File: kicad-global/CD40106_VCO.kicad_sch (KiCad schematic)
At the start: 46 parts, among them J1 1V/Oct, J2 FM, J3 PWM_CV, J4 Saw, J5 Square, Q1 BC558, Q2 BC548, U1 TL074, U2 40106

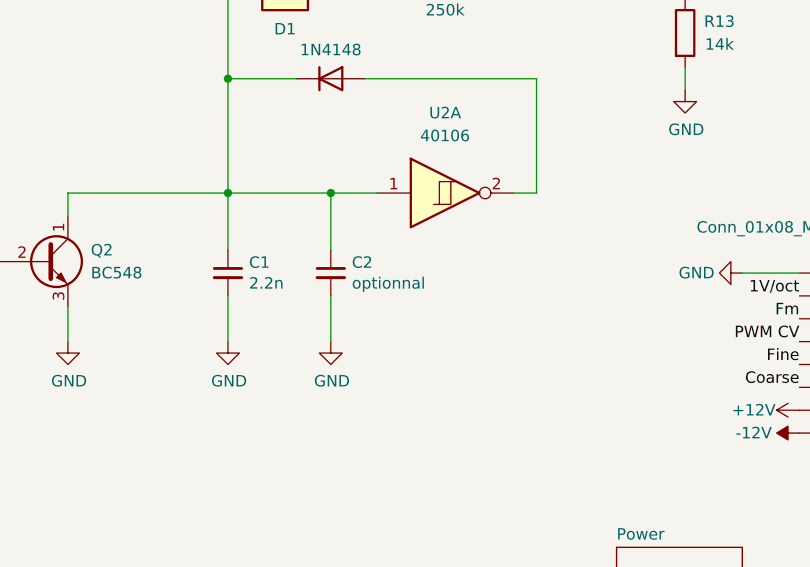
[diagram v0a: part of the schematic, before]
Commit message: update components
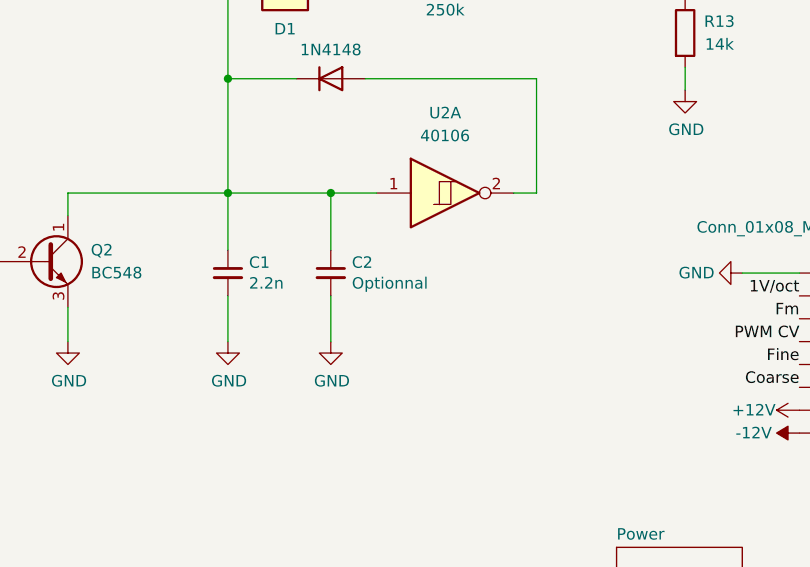
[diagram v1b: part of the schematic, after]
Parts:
- C1: footprint Capacitor_THT:C_Disc_D7.0mm_W2.5mm_P5.00mm -> Capacitor_THT:C_Rect_L7.0mm_W6.5mm_P5.00mm; Comments (none) -> Mica capacitor for stability; manf (none) -> Cornell Dubilier; manf# (none) -> CD16FD222JO3F
- C2: value optionnal -> Optionnal; footprint Capacitor_THT:C_Disc_D7.0mm_W2.5mm_P5.00mm -> Capacitor_THT:C_Rect_L7.0mm_W6.5mm_P5.00mm; Comments (none) -> Mica capacitor for stability; manf (none) -> Cornell Dubilier; manf# (none) -> CD16FD222JO3F
- lvl_Trim: Comments (none) -> Use multi turn Cermet style 3296 pots
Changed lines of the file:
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@@
       (effects (font (size 1.27 1.27)) (justify left))
     )
-    (property "Footprint" "Capacitor_THT:C_Disc_D7.0mm_W2.5mm_P5.00mm" (at 133.35 119.38 0)
+    (property "Footprint" "Capacitor_THT:C_Rect_L7.0mm_W6.5mm_P5.00mm" (at 133.35 119.38 0)
       (effects (font (size 1.27 1.27)) hide)
     )
     (property "Datasheet" "~" (at 133.35 119.38 0)
+      (effects (font (size 1.27 1.27)) hide)
+    )
+    (property "manf" "Cornell Dubilier" (at 133.35 119.38 0)
+      (effects (font (size 1.27 1.27)) hide)
+    )
+    (property "manf#" "CD16FD222JO3F" (at 133.35 119.38 0)
+      (effects (font (size 1.27 1.27)) hide)
+    )
+    (property "Comments" "Mica capacitor for stability" (at 133.35 119.38 0)
       (effects (font (size 1.27 1.27)) hide)
     )
@@
     )
     (property "Datasheet" "~" (at 80.01 152.4 0)
+      (effects (font (size 1.27 1.27)) hide)
+    )
+    (property "manf" "" (at 80.01 152.4 90)
+      (effects (font (size 1.27 1.27)) hide)
+    )
+    (property "manf#" "" (at 80.01 152.4 90)
+      (effects (font (size 1.27 1.27)) hide)
+    )
+    (property "Comments" "Use multi turn Cermet style 3296 pots " (at 80.01 152.4 90)
       (effects (font (size 1.27 1.27)) hide)
     )
@@
     )
   )
-  (symbol (lib_id "Device:C_Small") (at 144.78 119.38 0) (unit 1)
-    (in_bom yes) (on_board yes) (dnp no)
-    (property "Reference" "C2" (at 147.1168 118.2116 0)
-      (effects (font (size 1.27 1.27)) (justify left))
-    )
-    (property "Value" "optionnal" (at 147.1168 120.523 0)
-      (effects (font (size 1.27 1.27)) (justify left))
-    )
-    (property "Footprint" "Capacitor_THT:C_Disc_D7.0mm_W2.5mm_P5.00mm" (at 144.78 119.38 0)
-      (effects (font (size 1.27 1.27)) hide)
-    )
-    (property "Datasheet" "~" (at 144.78 119.38 0)
-      (effects (font (size 1.27 1.27)) hide)
-    )
-    (pin "1")
-    (pin "2")
-    (instances
-      (project "CD40106_VCO"
-        (path "/fea7c5d1-76d6-41a0-b5e3-29889dbb8ce0"
-          (reference "C2") (unit 1)
-        )
-      )
-    )
-  )
   (symbol (lib_id "Transistor_BJT:BC558") (at 96.52 125.73 0) (unit 1)
     (in_bom yes) (on_board yes) (dnp no) (fields_autoplaced)
@@
         )
       )
+    )
+  )
+  (symbol (lib_id "Device:C_Small") (at 144.78 119.38 0) (unit 1)
+    (in_bom yes) (on_board yes) (dnp no)
+    (property "Reference" "C2" (at 147.1168 118.2116 0)
+      (effects (font (size 1.27 1.27)) (justify left))
+    )
+    (property "Value" "Optionnal" (at 147.1168 120.523 0)
+      (effects (font (size 1.27 1.27)) (justify left))
+    )
+    (property "Footprint" "Capacitor_THT:C_Rect_L7.0mm_W6.5mm_P5.00mm" (at 144.78 119.38 0)
+      (effects (font (size 1.27 1.27)) hide)
+    )
+    (property "Datasheet" "~" (at 144.78 119.38 0)
+      (effects (font (size 1.27 1.27)) hide)
+    )
+    (property "manf" "Cornell Dubilier" (at 144.78 119.38 0)
+      (effects (font (size 1.27 1.27)) hide)
+    )
+    (property "manf#" "CD16FD222JO3F" (at 144.78 119.38 0)
+      (effects (font (size 1.27 1.27)) hide)
+    )
+    (property "Comments" "Mica capacitor for stability" (at 144.78 119.38 0)
+      (effects (font (size 1.27 1.27)) hide)
+    )
+    (pin "1")
+    (pin "2")
+    (instances
+      (project "CD40106_VCO"
+        (path "/fea7c5d1-76d6-41a0-b5e3-29889dbb8ce0"
+          (reference "C2") (unit 1)
+        )
+      )

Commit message: finished v1 of module
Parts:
- removed J1: 1V/Oct, Synth:Thonkiconn, symbol Connector:AudioJack2_SwitchT
- removed J2: FM, Synth:Thonkiconn, symbol Connector:AudioJack2_SwitchT
- removed J3: PWM_CV, Synth:Thonkiconn, symbol Connector:AudioJack2_SwitchT
- removed J4: Saw, Synth:Thonkiconn, symbol Connector:AudioJack2_SwitchT
- removed J5: Square, Synth:Thonkiconn, symbol Connector:AudioJack2_SwitchT
- removed J? (x2): Conn_01x08_Female, Connector_PinSocket_2.54mm:PinSocket_1x08_P2.54mm_Vertical, symbol Connector:Conn_01x08_Female
- removed J? (x2): Conn_01x08_Male, Connector_PinHeader_2.54mm:PinHeader_1x08_P2.54mm_Vertical, symbol Connector:Conn_01x08_Male
- added D1: 1N4148, Diode_THT:D_DO-35_SOD27_P7.62mm_Horizontal, symbol Device:D
- added J13: PWM_CV, Kicad-perso:Thonkiconn, symbol Kicad-perso:AudioJack_Switch
- added J13: CV, Kicad-perso:Thonkiconn, symbol Kicad-perso:AudioJack_Switch
- added J13: Square, Kicad-perso:Thonkiconn, symbol Kicad-perso:AudioJack_Switch
- added J13: Sync, Kicad-perso:Thonkiconn, symbol Kicad-perso:AudioJack_Switch
- added J13: Saw, Kicad-perso:Thonkiconn, symbol Kicad-perso:AudioJack_Switch
- added J13: FM, Kicad-perso:Thonkiconn, symbol Kicad-perso:AudioJack_Switch
- added J3 (x2): Conn_Circuit, Connector_PinSocket_2.54mm:PinSocket_1x08_P2.54mm_Vertical, symbol Connector_Generic:Conn_01x08
- added J5 (x2): Conn_Jack, Connector_PinHeader_2.54mm:PinHeader_1x08_P2.54mm_Vertical, symbol Connector_Generic:Conn_01x08
- added TP1 (x2): TestPoint, TestPoint:TestPoint_Plated_Hole_D2.0mm, symbol Connector:TestPoint
- C1: value 2.2n -> 2.2nF; footprint Capacitor_THT:C_Rect_L7.0mm_W6.5mm_P5.00mm -> Kicad-perso:Mica Disc Cap
- C2: footprint Capacitor_THT:C_Rect_L7.0mm_W6.5mm_P5.00mm -> Capacitor_THT:C_Disc_D7.0mm_W2.5mm_P5.00mm; Comments Mica capacitor for stability -> If you don't have a mica capacitor, just use a regular cera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; manf Cornell Dubilier -> (none); manf# CD16FD222JO3F -> (none)
- C3: value 1u -> 1uF
- FM_LVL1, PWM1, PWM_CV_LVL1: footprint Synth:Pot-bourns-alpha -> Kicad-perso:Pot-bourns-alpha
- H3: renamed from H1; footprint Synth:Doepfer Mounting hole -> Kicad-perso:Doepfer Mounting hole
- H4: renamed from H2; footprint Synth:Doepfer Mounting hole -> Kicad-perso:Doepfer Mounting hole
- H5: renamed from H3; footprint Synth:Doepfer Mounting hole -> Kicad-perso:Doepfer Mounting hole
- H6: renamed from H4; footprint Synth:Doepfer Mounting hole -> Kicad-perso:Doepfer Mounting hole
- TH1, TH2, TH3, TH4: footprint (none) -> Kicad-perso:Therm_Disc_D6.5mm_W2.5mm_P3.50mm; manf (none) -> THINKING; manf# (none) -> ATTC-5100
- U2: value 40106 -> CD40106; footprint (none) -> Package_DIP:DIP-14_W7.62mm_LongPads; manf (none) -> Nexperia; manf# (none) -> CD40106BE
- gave numbers to parts that had none: 2
- renumbered D1 to D2, R4 to R1, R13 to R10, R14 to R11, R15 to R12, R16 to R13, R17 to R14, R18 to R15, R5 to R2, R6 to R3, R7 to R4, R8 to R5, R9 to R6, R10 to R7, R11 to R8, R12 to R9, lvl_Trim to lvl_Trim1
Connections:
- net Octave switch/Fine is gone; now on net Fine: R2.2
- net +12V: now also PWM1.3, J3.7 (Pin_7), J5.7 (Pin_7); no longer PWM1.1
- net -12V: now also PWM1.1, J3.8 (Pin_8), J5.8 (Pin_8); no longer PWM1.3
- net 1V/oct: now also J13.T, J3.2 (Pin_2), J5.2 (Pin_2)
- net Fine: now also J3.5 (Pin_5), J5.5 (Pin_5)
- net Fm: now also J3.3 (Pin_3), J5.3 (Pin_3)
- net GND: now also J13.S, J13.S, J13.S, J13.S, J13.S, J13.S, J13.TN, J13.TN, J13.TN, J3.1 (Pin_1), J3.1 (Pin_1), J3.8 (Pin_8), J5.1 (Pin_1), J5.1 (Pin_1), J5.8 (Pin_8)
- net PWM: now also J3.2 (Pin_2), J5.2 (Pin_2)
- net PWM CV: now also PWM_CV_LVL1.1, J3.4 (Pin_4), J5.4 (Pin_4); no longer PWM_CV_LVL1.3
- net Saw out: now also J13.T, J3.4 (Pin_4), J5.4 (Pin_4)
- net Square out: now also J13.T, J3.3 (Pin_3), J5.3 (Pin_3)
- net Sync: now reaches C1.1, C2.1, D2.1 (K), Q2.1 (C), U1.3 (+), U2.1
- net Sync: now also D1.1 (K), J3.7 (Pin_7), J5.7 (Pin_7), TP1.1
- net at FM_LVL1.1: now also J13.T
- net at Q1.2 (B), R5.1, TH1.2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: now also TP1.1
- net Octave switch/Octave renamed octave
- new net: J13.T, PWM_CV_LVL1.3
- new net: D1.2 (A), J13.T
- new net Fine_oct_in: J3.6 (Pin_6), J5.6 (Pin_6)
- new net Sine out: J3.5 (Pin_5), J5.5 (Pin_5)
- new net Tri out: J3.6 (Pin_6), J5.6 (Pin_6)
- no-connect marks 5 -> 3
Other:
- sheet Octave switch ports: added Fine_oct_in; removed none
- sheet Wave Converter ports: added Sine out, Tri out; removed none
- moved on the sheet: C1, PWM_CV_LVL1, R7, R8

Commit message: doc + fab files for V1.0
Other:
- company: (none) -> Bleep Sound
- title: (none) -> CD40106 VCO
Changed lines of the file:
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@@
 (kicad_sch (version 20230121) (generator eeschema)
   (paper "A4")
+  (title_block
+    (title "CD40106 VCO")
+    (date "2023-12-10")
+    (rev "1.0")
+    (company "Bleep Sound")
+  )
   (junction (at 232.41 44.45) (diameter 0) (color 0 0 0 0)
   )

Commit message: First proto fix
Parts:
- removed C1: 2.2nF, Kicad-perso:Mica Disc Cap, symbol Device:C_Small
- added R41: 1k, Resistor_THT:R_Axial_DIN0207_L6.3mm_D2.5mm_P10.16mm_Horizontal, symbol Device:R
- C2: value Optionnal -> 2.2nF
- FM_LVL1: value 1M -> B1M
- PWM1: value 100k -> B100k
- PWM_CV_LVL1: value 250k -> B250k
- R13: value 1M -> 100k
- renumbered J13 to J1, J13 to J10, J13 to J2, J13 to J3, J13 to J4, J3 to J5, J5 to J6, J3 to J7, J5 to J8, J13 to J9, TP1 to TP2
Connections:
- net -12V: now also Q1.1 (C); no longer Q1.3 (E)
- net Square out: now also R41.2; no longer J10.T
- net at Q2.2 (B), R6.2: now also Q1.3 (E); no longer Q1.1 (C)
- new net: J10.T, R41.1
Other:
- moved on the sheet: C2, J10

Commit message: V2.0
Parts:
- added C1: 470pF, Capacitor_THT:C_Disc_D7.0mm_W2.5mm_P5.00mm, symbol Device:C_Small
- added Q3: BC548, Package_TO_SOT_THT:TO-92_Inline, symbol Transistor_BJT:BC548
- added Q4: BC558, Package_TO_SOT_THT:TO-92_Inline, symbol Transistor_BJT:BC558
- added R46: 47k, Resistor_THT:R_Axial_DIN0207_L6.3mm_D2.5mm_P10.16mm_Horizontal, symbol Device:R
- added R47: 2.2k, Resistor_THT:R_Axial_DIN0207_L6.3mm_D2.5mm_P10.16mm_Horizontal, symbol Device:R
- added R48: 10k, Resistor_THT:R_Axial_DIN0207_L6.3mm_D2.5mm_P10.16mm_Horizontal, symbol Device:R
- C2: footprint Capacitor_THT:C_Disc_D7.0mm_W2.5mm_P5.00mm -> Capacitor_THT:C_Rect_L7.0mm_W2.5mm_P5.00mm; Comments If you don't have a mica capacitor, just use a regular cera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 -> If you don't have a mylar capacitor, just use a regular cer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; Links (none) -> https://www.taydaelectronics.com/capacitors/2-2nf-0-0022uf-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
- C3: Links (none) -> https://www.taydaelectronics.com/capacitors/monolithic-cera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
- D1, D2: Links (none) -> https://www.taydaelectronics.com/1n4148-switching-signal-di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
- FM_LVL1, PWM1, PWM_CV_LVL1: Links (none) -> https://www.thonk.co.uk/shop/alpha-9mm-pots/
- J1, J10, J2, J3, J4, J9: Comments Thonkiconn jack -> (none); Links (none) -> https://www.thonk.co.uk/shop/thonkiconn/
- Q1: Links (none) -> https://www.taydaelectronics.com/bc558-bc558b-transistor-pn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
- Q2: Links (none) -> https://www.taydaelectronics.com/bc548-transistor-npn-30v-0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
- R1, R10, R11, R12, R13, R14, R15, R2, R3, R4, R41, R5, R6, R7, R8, R9: Links (none) -> https://www.taydaelectronics.com/resistors/1-4w-metal-film-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
- TH1, TH2, TH3, TH4: Links (none) -> https://www.taydaelectronics.com/10k-ohm-ntc-thermistor-5mm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
- U1: Links (none) -> https://www.thonk.co.uk/shop/eurorack-diy-essentials/; manf (none) -> Texas Instrument; manf# (none) -> TL074CN
- U2: Links (none) -> https://eu.mouser.com/ProductDetail/Texas-Instruments/CD401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
- lvl_Trim1: footprint Potentiometer_THT:Potentiometer_Bourns_3386C_Horizontal -> Potentiometer_THT:Potentiometer_Bourns_3296W_Vertical; Comments Use multi turn Cermet style 3296 pots -> (none); Links (none) -> Trimmer potentiometer, 25 turn series 3296W
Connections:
- net +12V: now also Q4.3 (E), R47.1
- net GND: now also D1.2 (A), Q3.3 (E), R46.2
- net Sync: now also C1.2, Q3.2 (B), R46.1; no longer C2.1, D2.1 (K), Q2.1 (C), TP2.1, U1.3 (+), U2.1
- net at J3.T: now also C1.1; no longer D1.2 (A)
- new net: C2.1, D2.1 (K), Q2.1 (C), Q4.1 (C), TP2.1, U1.3 (+), U2.1
- new net: Q3.1 (C), R48.2
- new net: Q4.2 (B), R47.2, R48.1
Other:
- moved on the sheet: D1, FM_LVL1, J1, J2, J3, R1, R2, R3, R4, R5, TH1, TH2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
